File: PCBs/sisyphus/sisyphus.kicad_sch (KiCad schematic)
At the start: 43 parts, among them J1 USB_C_Receptacle_USB2.0_14P, J2 AUX USB, J3 Conn_01x02, J4 Speaker, J5 SWD, J6 RGB_CONN, J7 Keyboard, J8 Light sensor, U1 NCP1117-3.3_SOT223, U2 USBLC6-2P6, U3 W25Q128JVS, U4 MAX98357A, U5 RP2040, Y1 ABM8-272-T3

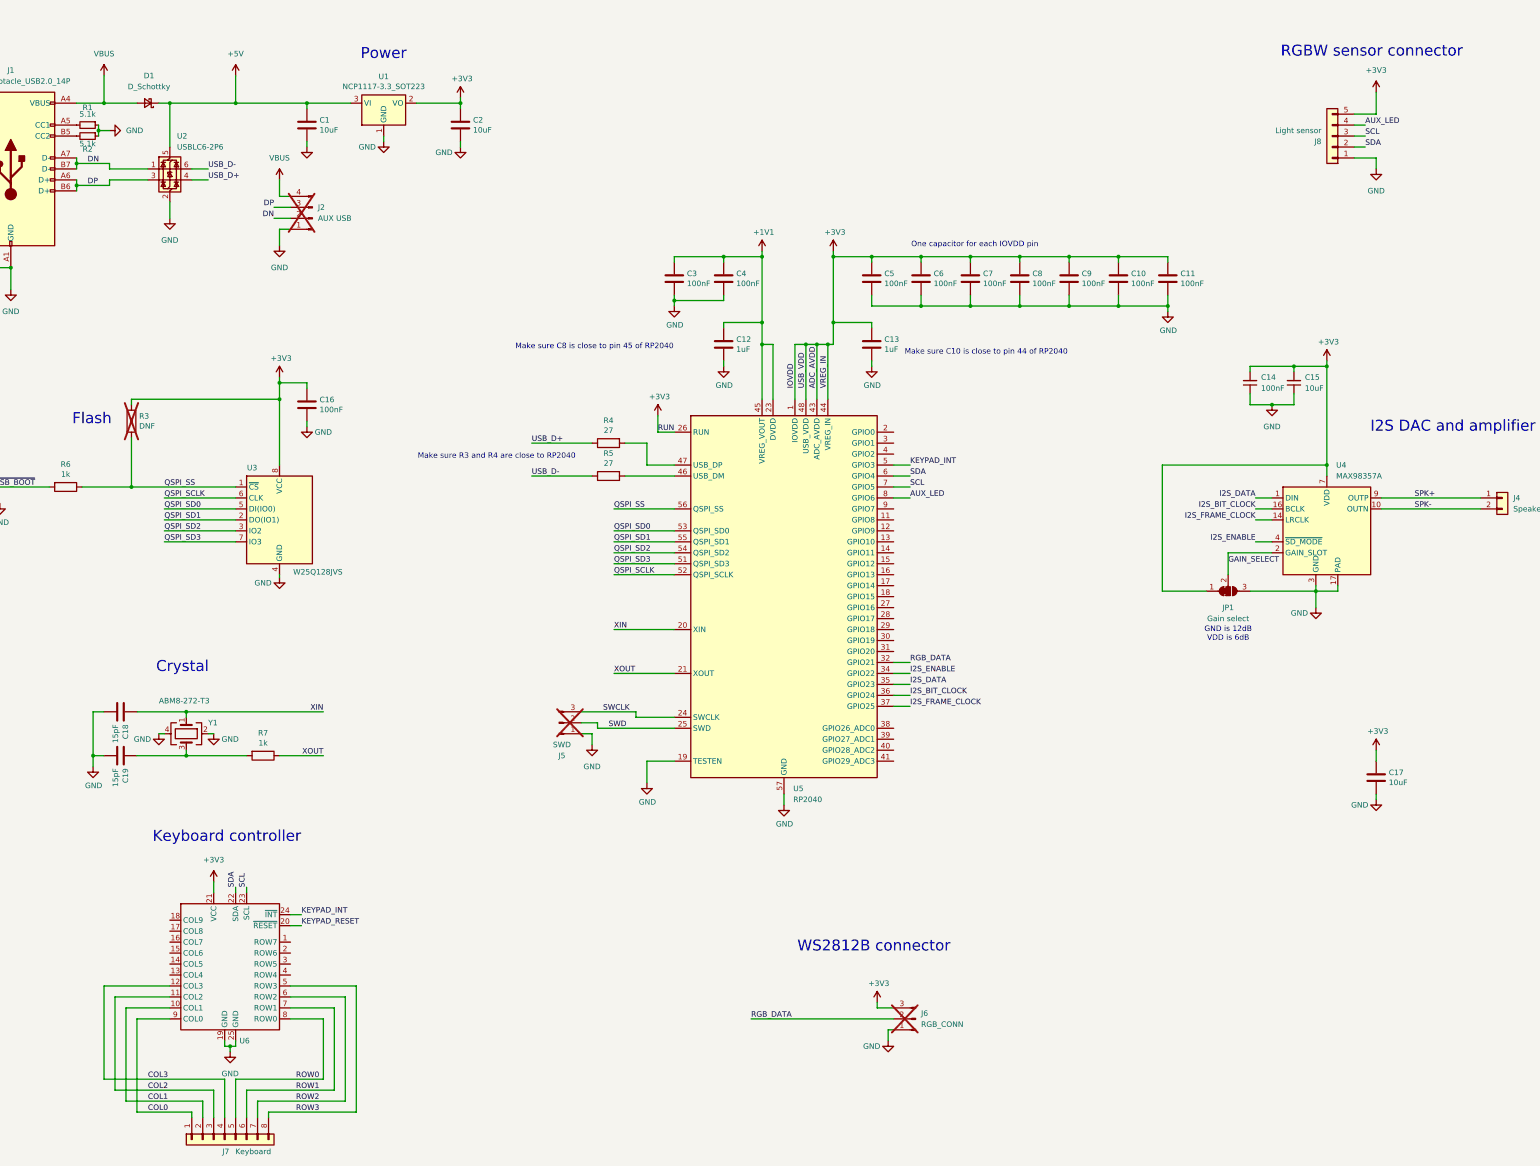
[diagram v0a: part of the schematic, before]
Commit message: Add battery testing battery charger implementation Also remove unncessary tracked files
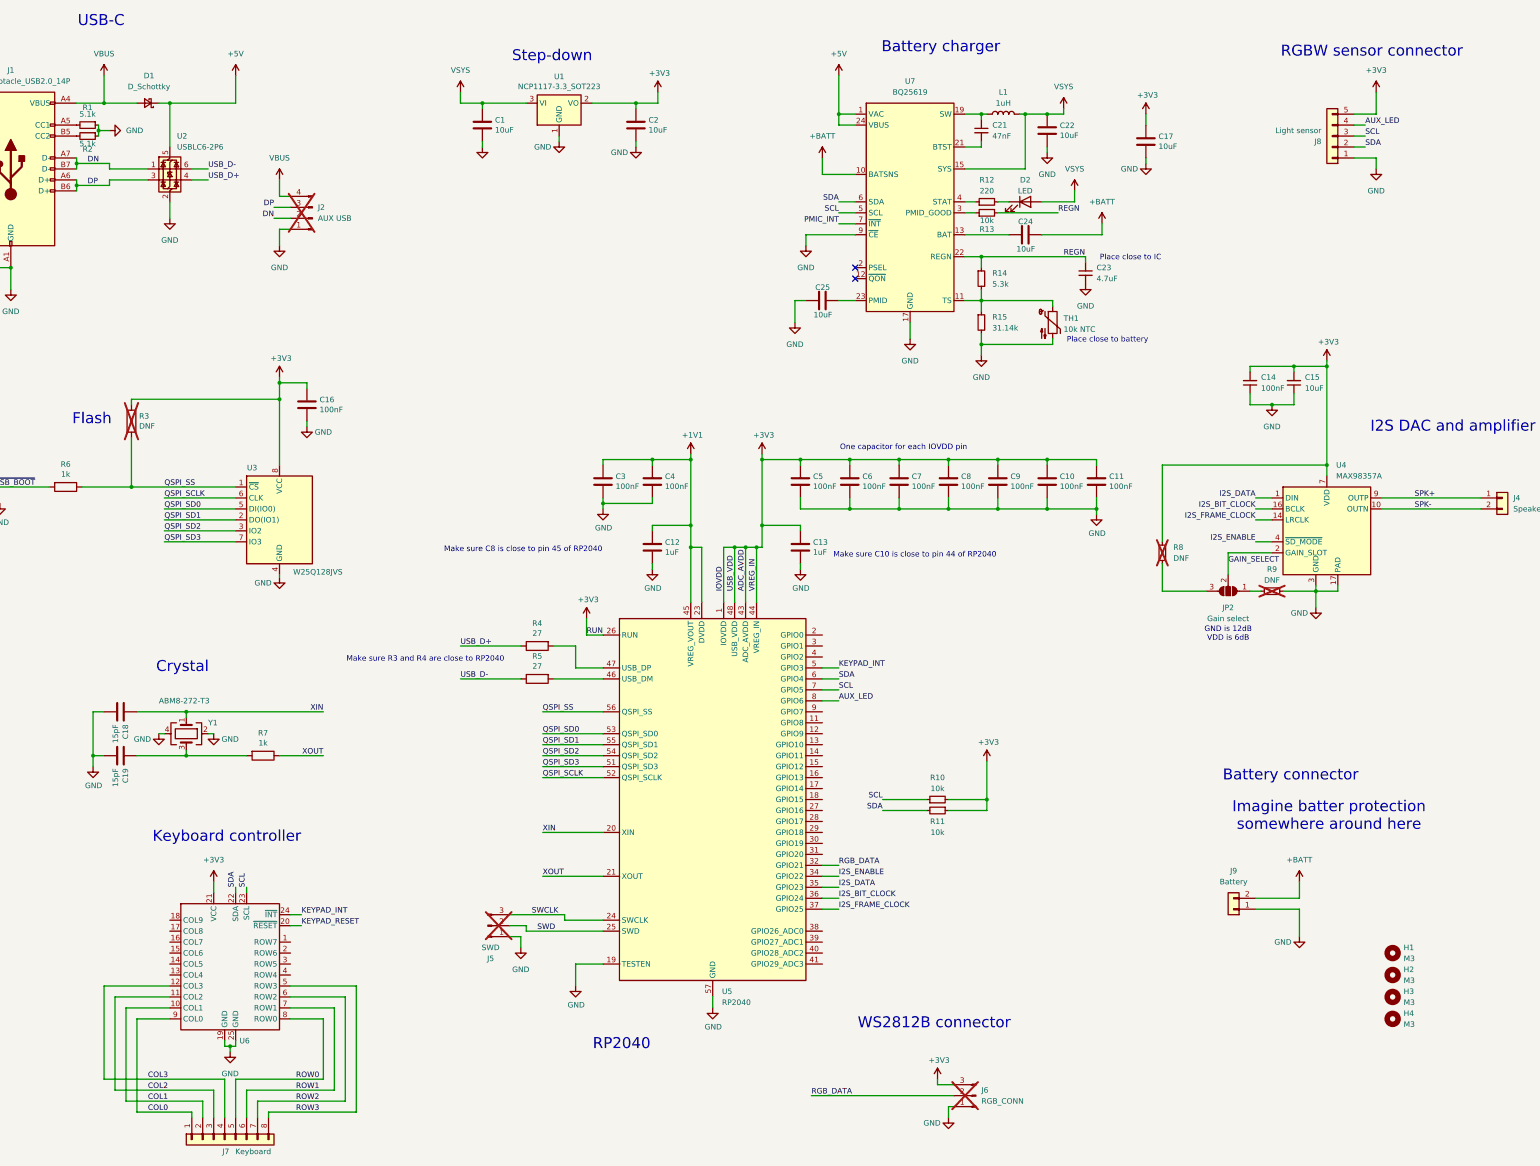
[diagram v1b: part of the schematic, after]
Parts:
- removed JP1: Gain select, Jumper:SolderJumper-3_P1.3mm_Bridged12_RoundedPad1.0x1.5mm, symbol Jumper:SolderJumper_3_Bridged12
- added C21: 47nF, Capacitor_SMD:C_0402_1005Metric, symbol Device:C_Small
- added C22, C24, C25: 10uF, Capacitor_SMD:C_0805_2012Metric, symbol Device:C
- added C23: 4.7uF, Capacitor_SMD:C_0402_1005Metric, symbol Device:C_Small
- added D2: LED, LED_SMD:LED_0402_1005Metric, symbol Device:LED
- added H1, H2, H3, H4: M3, MountingHole:MountingHole_3.2mm_M3_ISO7380, symbol Mechanical:MountingHole
- added J9: Battery, Connector_JST:JST_PH_S2B-PH-SM4-TB_1x02-1MP_P2.00mm_Horizontal, symbol Connector_Generic:Conn_01x02
- added JP2: Gain select, Jumper:SolderJumper-3_P1.3mm_Open_RoundedPad1.0x1.5mm, symbol Jumper:SolderJumper_3_Open
- added L1: 1uH, Inductor_SMD:L_0402_1005Metric, symbol Device:L
- added R10, R11, R13: 10k, Resistor_SMD:R_0402_1005Metric, symbol Device:R_Small
- added R12: 220, Resistor_SMD:R_0402_1005Metric, symbol Device:R_Small
- added R14: 5.3k, Resistor_SMD:R_0402_1005Metric, symbol Device:R_Small
- added R15: 31.14k, Resistor_SMD:R_0402_1005Metric, symbol Device:R_Small
- added R8, R9: DNF, Resistor_SMD:R_0402_1005Metric, symbol Device:R_Small
- added TH1: 10k NTC, Connector_PinHeader_2.54mm:PinHeader_1x02_P2.54mm_Vertical, symbol Device:Thermistor_NTC
- added U7: BQ25619, Package_DFN_QFN:Texas_RTW_WQFN-24-1EP_4x4mm_P0.5mm_EP2.7x2.7mm_ThermalVias, symbol Sisyphus:BQ25619
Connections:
- net +3V3: now also R10.2, R11.1, R8.1
- net +5V: now also U7.1 (VAC), U7.24 (VBUS); no longer C1.1, U1.3 (VI)
- net GAIN_SELECT: now also JP2.2 (C)
- net GND: now also C22.2, C23.2, C25.1, J9.1 (Pin_1), R15.2, R9.2, TH1.2, U7.17 (GND), U7.18 (GND), U7.25 (GND), U7.9 (~{CE})
- net SCL: now also R10.1, U7.5 (SCL)
- net SDA: now also R11.2, U7.6 (SDA)
- new net: R12.1, U7.4 (STAT)
- new net: D2.1 (K), R12.2
- new net: R14.2, R15.1, TH1.1, U7.11 (TS)
- new net: C24.1, U7.13 (BAT), U7.14 (BAT)
- new net: C21.1, L1.1, U7.19 (SW), U7.20 (SW)
- new net: C21.2, U7.21 (BTST)
- new net: C25.2, U7.23 (PMID)
- new net: R13.1, U7.3 (PMID_GOOD)
- new net: JP2.1 (A), R9.1
- new net: JP2.3 (B), R8.2
- new net +BATT: C24.2, J9.2 (Pin_2), U7.10 (BATSNS)
- new net PMIC_INT: U7.7 (~{INT})
- new net REGN: C23.1, R13.2, R14.1, U7.22 (REGN)
- new net VSYS: C1.1, C22.1, D2.2 (A), L1.2, U1.3 (VI), U7.15 (SYS), U7.16 (SYS)
- no-connect marks 0 -> 2
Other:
- note added: "Battery charger"
- note added: "Battery connector"
- note added: "Imagine batter protection somewhere around here"
- note added: "Place close to IC"
- note added: "Place close to battery"
- note added: "RP2040"
- note added: "Step-down"
- note added: "USB-C"
- note removed: "Power"
- moved on the sheet: C1, C10, C11, C12, C13, C17, C2, C3, C4, C5, C6, C7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

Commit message: Update main PCB
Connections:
- net +BATT: now also C24.1, U7.13 (BAT), U7.14 (BAT); no longer C24.2
- net GND: now also C24.2
- net SW: now reaches C21.1, L1.1, U7.19 (SW), U7.20 (SW)
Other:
- moved on the sheet: C24
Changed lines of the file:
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@@
 	(text "Place close to IC"
 		(exclude_from_sim no)
-		(at 294.894 72.644 0)
+		(at 275.59 74.422 0)
 		(effects
 			(font
@@
 	)
 	(junction
+		(at 288.29 67.31)
+		(diameter 0)
+		(color 0 0 0 0)
+	)
+	(junction
 		(at 180.34 36.83)
 		(diameter 0)
@@
 	(wire
 		(pts
+			(xy 288.29 67.31) (xy 298.45 67.31)
+		)
+		(stroke
+			(width 0)
+			(type default)
+		)
+	)
+	(wire
+		(pts
 			(xy 203.2 139.7) (xy 205.74 139.7)
 		)
@@
 	(wire
 		(pts
-			(xy 274.32 67.31) (xy 288.29 67.31)
-		)
-		(stroke
-			(width 0)
-			(type default)
-		)
-	)
-	(wire
-		(pts
 			(xy 170.18 36.83) (xy 180.34 36.83)
 		)
@@
 	(wire
 		(pts
-			(xy 256.54 67.31) (xy 266.7 67.31)
+			(xy 256.54 67.31) (xy 288.29 67.31)
 		)
 		(stroke
@@
 	(wire
 		(pts
+			(xy 298.45 67.31) (xy 298.45 68.58)
+		)
+		(stroke
+			(width 0)
+			(type default)
+		)
+	)
+	(wire
+		(pts
 			(xy 100.33 243.84) (xy 113.03 243.84)
 		)
@@
 	(wire
 		(pts
+			(xy 298.45 76.2) (xy 298.45 77.47)
+		)
+		(stroke
+			(width 0)
+			(type default)
+		)
+	)
+	(wire
+		(pts
 			(xy 237.49 198.12) (xy 247.65 198.12)
 		)
@@
 		)
 	)
+	(label "SW"
+		(at 257.81 39.37 0)
+		(effects
+			(font
+				(size 1.27 1.27)
+			)
+			(justify left bottom)
+		)
+	)
 	(label "DN"
 		(at 96.52 63.5 180)
@@
 	)
 	(symbol
+		(lib_name "GND_8")
+		(lib_id "power:GND")
+		(at 298.45 77.47 0)
+		(unit 1)
+		(exclude_from_sim no)
+		(in_bom yes)
+		(on_board yes)
+		(dnp no)
+		(fields_autoplaced yes)
+		(property "Reference" "#PWR055"
+			(at 298.45 83.82 0)
+			(effects
+				(font
+					(size 1.27 1.27)
+				)
+				(hide yes)
+			)
+		)
+		(property "Value" "GND"
+			(at 298.45 82.55 0)
+			(effects
+				(font
+					(size 1.27 1.27)
+				)
+			)
+		)
+		(property "Footprint" ""
+			(at 298.45 77.47 0)
+			(effects
+				(font
+					(size 1.27 1.27)
+				)
+				(hide yes)
+			)
+		)
+		(property "Datasheet" ""
+			(at 298.45 77.47 0)
+			(effects
+				(font
+					(size 1.27 1.27)
+				)
+				(hide yes)
+			)
+		)
+		(property "Description" "Power symbol creates a global label with name \"GND\" , ground"
+			(at 298.45 77.47 0)
+			(effects
+				(font
+					(size 1.27 1.27)
+				)
+				(hide yes)
+			)
+		)
+		(pin "1"
+		)
+		(instances
+			(project "sisyphus"
+				(path "/8c0b3d8b-46d3-4173-ab1e-a61765f77d61"
+					(reference "#PWR055")
+					(unit 1)
+				)
+			)
+		)
+	)
+	(symbol
 		(lib_id "Device:R_Small")
 		(at 250.19 198.12 90)
@@
 	(symbol
 		(lib_id "Device:C")
-		(at 270.51 67.31 90)
+		(at 298.45 72.39 0)
 		(unit 1)
 		(exclude_from_sim no)
@@
 		(dnp no)
 		(property "Reference" "C24"
-			(at 272.288 64.262 90)
+			(at 301.244 71.374 0)
 			(effects
 				(font
@@
 		)
 		(property "Value" "10uF"
-			(at 272.796 70.612 90)
+			(at 300.99 73.406 0)
 			(effects
 				(font
@@
 		)
 		(property "Footprint" "Capacitor_SMD:C_0805_2012Metric"
-			(at 274.32 66.3448 0)
+			(at 299.4152 76.2 0)
 			(effects
 				(font
@@
 		)
 		(property "Datasheet" "~"
-			(at 270.51 67.31 0)
+			(at 298.45 72.39 0)
 			(effects
 				(font
@@
 		)
 		(property "Description" ""
-			(at 270.51 67.31 0)
+			(at 298.45 72.39 0)
 			(effects
 				(font

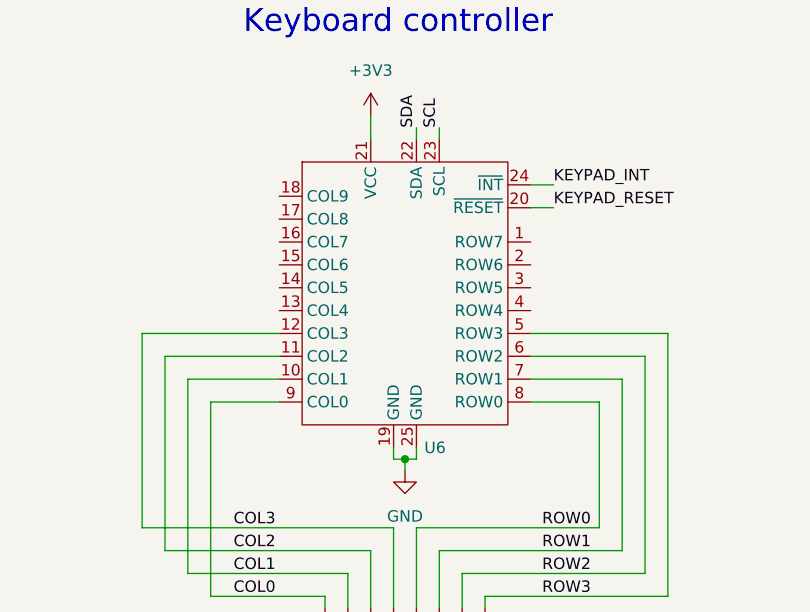
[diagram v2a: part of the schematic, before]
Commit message: Fix background on chip symbols
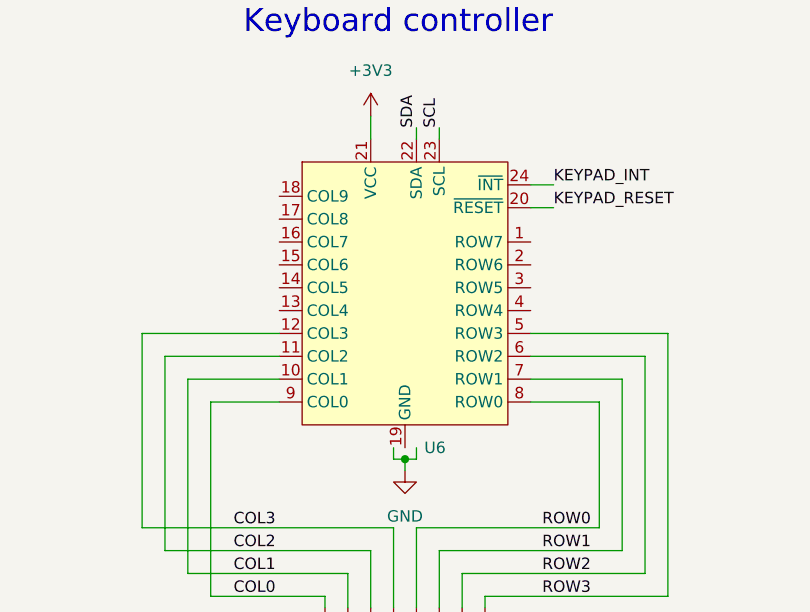
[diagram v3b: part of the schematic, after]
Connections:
- net GND: no longer U6.19 (GND), U6.25 (GND)
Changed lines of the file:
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@@
 		(pin "12"
-		)
-		(pin "25"
 		)
 		(instances

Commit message: Major PCB update
I won't even bother commenting it
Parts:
- removed C1, C2: 10uF, Capacitor_SMD:C_0805_2012Metric, symbol Device:C
- removed R9: DNF, Resistor_SMD:R_0402_1005Metric, symbol Device:R_Small
- removed U1: NCP1117-3.3_SOT223, Package_TO_SOT_SMD:SOT-223-3_TabPin2, symbol Regulator_Linear:NCP1117-3.3_SOT223
- added C20: 100nF, Capacitor_SMD:C_0402_1005Metric, symbol Device:C_Small
- added C26, C27: 10uF, Capacitor_SMD:C_0402_1005Metric, symbol Device:C
- added J10: Limit SW, Connector_PinSocket_2.54mm:PinSocket_1x02_P2.54mm_Vertical, symbol Connector_Generic:Conn_01x02
- added L7: 2.2uH 1A, Inductor_SMD:L_0603_1608Metric, symbol Device:L
- added Q1: FS8205, Package_TO_SOT_SMD:SOT-23-6, symbol easyeda2kicad:FS8205
- added R16: 100, Resistor_SMD:R_0402_1005Metric, symbol Device:R_Small
- added R17: 1k, Resistor_SMD:R_0402_1005Metric, symbol Device:R_Small
- added U10: TPS62293, Package_SON:WSON-6-1EP_2x2mm_P0.65mm_EP1x1.6mm_ThermalVias, symbol Sisyphus:TPS62293
- added U8: DW01A, Package_TO_SOT_SMD:SOT-23-6, symbol Battery_Management:DW01A
- C15, C17, C22, C24, C25: footprint Capacitor_SMD:C_0805_2012Metric -> Capacitor_SMD:C_0402_1005Metric
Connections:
- net +3V3: now also C26.1, L7.1, U10.3 (FB); no longer C14.2, C15.2, R8.1, U4.7 (VDD), U4.8 (VDD)
- net +BATT: now also R16.1
- net AUX_LED: now also U5.31 (GPIO20); no longer U5.8 (GPIO6)
- net COL0: now also J7.5 (Pin_5); no longer J7.1 (Pin_1)
- net COL1: now also J7.6 (Pin_6); no longer J7.2 (Pin_2)
- net COL2: now also J7.7 (Pin_7); no longer J7.3 (Pin_3)
- net COL3: now also J7.8 (Pin_8); no longer J7.4 (Pin_4)
- net GAIN_SELECT: now also R8.1; no longer JP2.2 (C)
- net GND: now also JP2.1 (A), U6.19 (GND), U6.25 (PAD), C26.2, C27.2, J10.2 (Pin_2), Q1.1 (S1), R17.2, U10.2 (MODE), U10.6 (GND), U10.7 (PAD); no longer J9.1 (Pin_1)
- net I2S_BIT_CLOCK: now also U5.40 (GPIO28_ADC2); no longer U5.36 (GPIO24)
- net I2S_DATA: now also U5.39 (GPIO27_ADC1); no longer U5.35 (GPIO23)
- net I2S_ENABLE: now also U5.38 (GPIO26_ADC0); no longer U5.34 (GPIO22)
- net I2S_FRAME_CLOCK: now also U5.41 (GPIO29_ADC3); no longer U5.37 (GPIO25)
- net KEYPAD_INT: now also U5.17 (GPIO14); no longer U5.5 (GPIO3)
- net KEYPAD_RESET: now also U5.18 (GPIO15)
- net ROW0: now also J7.4 (Pin_4); no longer J7.5 (Pin_5)
- net ROW1: now also J7.3 (Pin_3); no longer J7.6 (Pin_6)
- net ROW2: now also J7.2 (Pin_2); no longer J7.7 (Pin_7)
- net ROW3: now also J7.1 (Pin_1); no longer J7.8 (Pin_8)
- net SCL: now also U5.37 (GPIO25); no longer U5.7 (GPIO5)
- net SDA: now also U5.36 (GPIO24); no longer U5.6 (GPIO4)
- net VSYS: now also C14.2, C15.2, JP2.3 (B), U4.7 (VDD), U4.8 (VDD), C27.1, U10.4 (EN), U10.5 (VIN)
- net at R8.2: now also JP2.2 (C); no longer JP2.3 (B)
- net LMT_SW: now reaches U5.30 (GPIO19)
- net LMT_SW: now also J10.1 (Pin_1)
- new net: C20.1, R16.2, U8.5 (VCC)
- new net: L7.2, U10.1 (SW)
- new net B-: C20.2, J9.1 (Pin_1), Q1.3 (S2), U8.6 (GND)
- new net CS: R17.1, U8.2 (CS)
- new net OC: Q1.6 (G1), U8.3 (OC)
- new net OD: Q1.4 (G2), U8.1 (OD)
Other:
- note added: "Decoupling for LEDs (and stuff)"
- note added: "Limit switch connector"
- note removed: "Imagine batter protection somewhere around here"
- moved on the sheet: C17, H1, H2, H3, H4, J9, JP2, R10, R11, R8

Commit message: Fix critical PCB errors
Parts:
- added C3: 1uF, Capacitor_SMD:C_0402_1005Metric, symbol Device:C_Small
- renumbered C21 to C1, C15 to C10, C16 to C11, C3 to C12, C4 to C13, C5 to C14, C6 to C15, C7 to C16, C8 to C17, C9 to C18, C10 to C19, C22 to C2, C11 to C20, C12 to C21, C13 to C22, C18 to C23, C19 to C24, C20 to C25, C17 to C26, C27 to C4, C26 to C5, C24 to C6, C23 to C7, C25 to C8, C14 to C9, J8 to J1, J7 to J10, J1 to J2, J2 to J3, J3 to J4, J4 to J5, J9 to J6, J5 to J7, J10 to J8, J6 to J9, JP2 to JP1, L7 to L2, R4 to R10, R5 to R11, R10 to R12, R11 to R13, R7 to R14, R16 to R15, R17 to R16, R12 to R3, R13 to R4, R14 to R5, R15 to R6, R3 to R7, R6 to R8, R8 to R9, U10 to U1, U7 to U3, U3 to U4, U4 to U5, U8 to U6, U5 to U7, U6 to U8
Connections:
- net +5V: now also C3.1
- net GND: now also C3.2
- net PMIC_INT: now also U7.29 (GPIO18)
- net VSYS: now also R3.2; no longer D2.2 (A)
- net at R3.1: now also D2.2 (A); no longer U3.4 (STAT)
- net at D2.1 (K): now also U3.4 (STAT); no longer R3.2
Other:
- moved on the sheet: D2, R3

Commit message: Add some ✨flair✨ to the PCB
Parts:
- removed H1, H2, H3, H4: M3, MountingHole:MountingHole_3.2mm_M3_ISO7380, symbol Mechanical:MountingHole
- added H1, H2, H3, H4: M3, MountingHole:MountingHole_3.2mm_M3_ISO7380_Pad, symbol Mechanical:MountingHole_Pad
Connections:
- net GND: now also H1.1, H2.1, H3.1, H4.1

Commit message: Add power switch
Minor changes
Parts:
- added Q1: AO3401A, Package_TO_SOT_SMD:SOT-23, symbol Transistor_FET:AO3401A
- added R1: 1M, Resistor_SMD:R_0402_1005Metric, symbol Device:R_Small
- added SW1: SW_SPDT_321, Connector_PinHeader_2.54mm:PinHeader_1x03_P2.54mm_Vertical, symbol Switch:SW_SPDT_321
- J4: value Conn_01x02 -> USB_BOOT
- renumbered Q1 to Q2, R9 to R10, R10 to R11, R11 to R12, R12 to R13, R13 to R14, R14 to R15, R15 to R16, R16 to R17, R1 to R2, R2 to R3, R3 to R4, R4 to R5, R5 to R6, R6 to R7, R7 to R8, R8 to R9
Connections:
- net GND: now also J4.1 (Pin_1), J8.1 (Pin_1), SW1.1 (C); no longer J4.2 (Pin_2), J8.2 (Pin_2)
- net LMT_SW: now also J8.2 (Pin_2); no longer J8.1 (Pin_1)
- net VSYS: now also Q1.3 (D); no longer C2.1, L1.2, R4.2, U3.15 (SYS), U3.16 (SYS)
- net ~{USB_BOOT}: now also J4.2 (Pin_2); no longer J4.1 (Pin_1)
- new net: Q1.1 (G), R1.1, SW1.2 (B)
- new net SYS: C2.1, L1.2, Q1.2 (S), R1.2, R4.2, U3.15 (SYS), U3.16 (SYS)
- no-connect marks 2 -> 3
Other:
- moved on the sheet: J4, J8
